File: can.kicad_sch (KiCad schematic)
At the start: 31 parts, among them J1401 Conn_01x03, U1401 MCP2518FD-xQBB, U1402 ISO7721DR, U1403 TCAN1044A-Q1, X1401 40 MHz

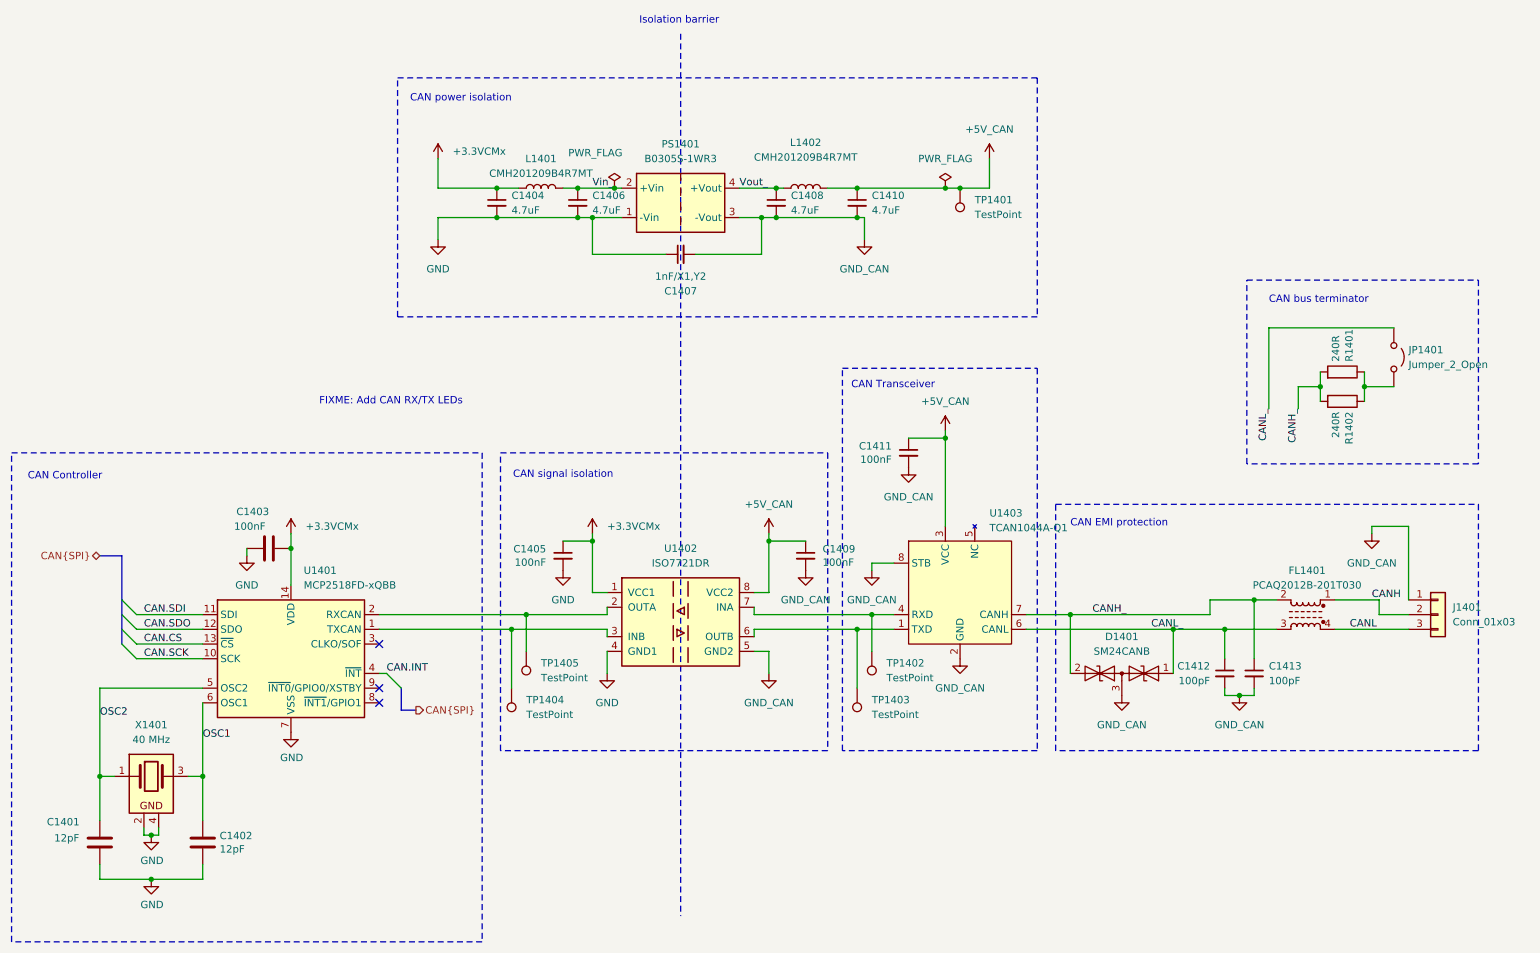
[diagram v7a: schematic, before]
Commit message: Partial trace layout, kick-ass custom rules
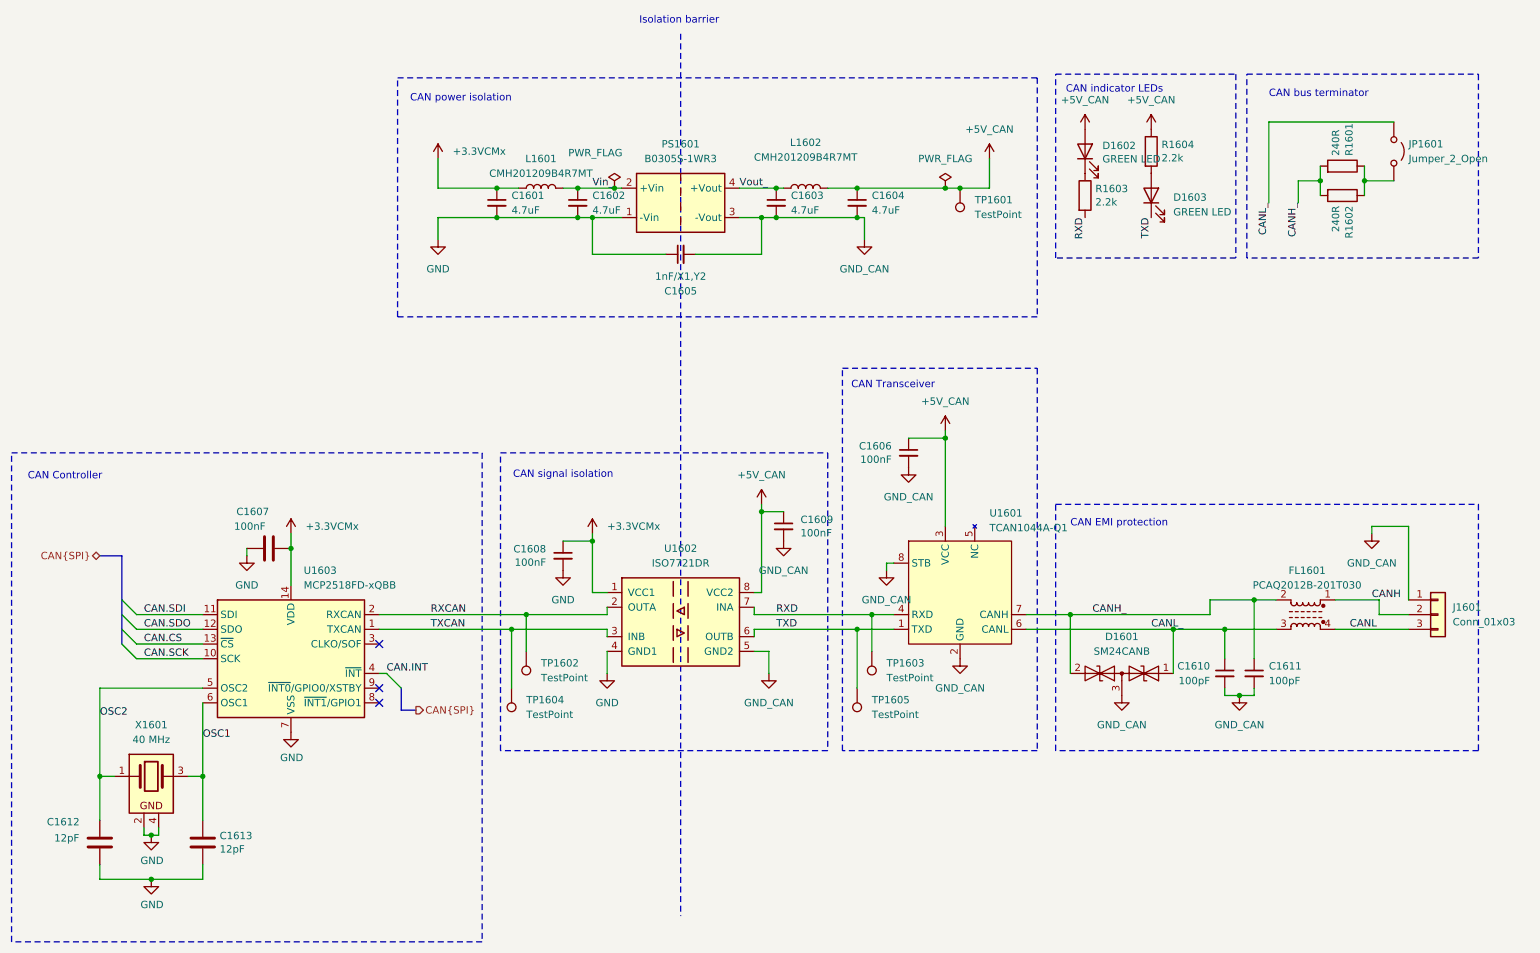
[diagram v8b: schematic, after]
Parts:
- added D1602, D1603: GREEN LED, LED_SMD:LED_0603_1608Metric, symbol Device:LED
- added R1603, R1604: 2.2k, Resistor_SMD:R_0402_1005Metric, symbol Device:R
- J1601: renamed from J1401; footprint Connector_PinHeader_2.54mm:PinHeader_1x03_P2.54mm_Vertical -> Connector_Phoenix_MC:PhoenixContact_MCV_1,5_3-G-3.81_1x03_P3.81mm_Vertical; LCSC C49257 -> C8389
- renumbered C1404 to C1601, C1406 to C1602, C1408 to C1603, C1410 to C1604, C1407 to C1605, C1411 to C1606, C1403 to C1607, C1405 to C1608, C1409 to C1609, C1412 to C1610, C1413 to C1611, C1401 to C1612, C1402 to C1613, D1401 to D1601, FL1401 to FL1601, JP1401 to JP1601, L1401 to L1601, L1402 to L1602, PS1401 to PS1601, R1401 to R1601, R1402 to R1602, TP1401 to TP1601, TP1405 to TP1602, TP1402 to TP1603, TP1404 to TP1604, TP1403 to TP1605, U1403 to U1601, U1402 to U1602, U1401 to U1603, X1401 to X1601
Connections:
- net +5V_CAN: now also D1602.2 (A), R1604.1
- net RXD: now reaches TP1603.1, U1601.4 (RXD), U1602.7 (INA)
- net RXD: now also R1603.2
- net TXCAN: now reaches TP1604.1, U1602.3 (INB), U1603.1 (TXCAN)
- net RXCAN: now reaches TP1602.1, U1602.2 (OUTA), U1603.2 (RXCAN)
- net TXD: now reaches TP1605.1, U1601.1 (TXD), U1602.6 (OUTB)
- net TXD: now also D1603.1 (K)
- new net: D1603.2 (A), R1604.2
- new net: D1602.1 (K), R1603.1
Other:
- note added: "CAN indicator LEDs"
- note removed: "FIXME: Add CAN RX/TX LEDs"
- moved on the sheet: C1609, JP1601, R1601, R1602
